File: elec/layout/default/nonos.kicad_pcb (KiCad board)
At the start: 2 copper layers, 4 parts, among them CN1 HRSHirose_DF40C_100DS_0_4V51, CN2 HRSHirose_DF40C_100DS_0_4V51, U1 _Texas_Instruments_SN74LVC1G0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

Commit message: refactor for core updates
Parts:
- added R1: , lcsc:R0402, F.Cu at (109.6, 28.8)
- added R2: 453Ω ±1% 62.5mW, lcsc:R0402, F.Cu at (104.4, 29.8)
- added RJ1: _HANRUNZhongshan_HanRun_Elec_HR911130A, lcsc:RJ45-TH_HR911130A, F.Cu at (168.2, 65.2)
- moved CN2 195.9 mm to (162.4, 104.6)
- moved CN1 145.0 mm to (125.6, 72.4)
- moved D1 112.4 mm to (103.8, 33.0)
- moved U1 34.0 mm to (138.4, 94.2)
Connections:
- net pins[23] renamed processor.hdi_b-pins[23]
- net pins[28] renamed processor.hdi_b-pins[28]
- net pins[33] renamed processor.hdi_b-pins[33]
- net pins[46] renamed processor-pins[46]
- net processor-signal-11 renamed pins[55]
- net processor.hdi_b-pins[38] renamed pins[38]
- net processor.hdi_b-pins[40] renamed pins[40]
- CN1 pad 12: processor-signal-3 -> processor-pins[23]
- CN1 pad 15: processor-signal-9 -> processor-signal-5
- CN1 pad 17: processor-signal-5 -> processor-pins[33]
- CN1 pad 22: processor-signal-1 -> pins[43]
- CN1 pad 23: processor-signal-10 -> processor-signal-8
- CN1 pad 24: pins[47] -> processor-signal-6
- CN1 pad 27: pins[53] -> processor-signal-3
- CN1 pad 29: processor-signal -> pins[57]
- CN1 pad 77: processor-signal-8 -> processor-pins[46]-1
- CN1 pad 78: processor-signal-6 -> processor-signal-2
- CN1 pad 80: processor-pins[40] -> processor-signal
- CN1 pad 81: processor-pins[38] -> processor-signal-9
- CN1 pad 82: processor-signal-12 -> processor-signal-7
- CN1 pad 85: processor-signal-7 -> processor-signal-4
- CN1 pad 86: processor-signal-4 -> processor-pins[28]
- CN1 pad 87: processor-signal-2 -> processor-signal-1
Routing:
- net (no net): track 5.67 -> 0.00 mm, vias 55 -> 0
- net GND: track 0.48 -> 0.00 mm, vias 35 -> 0

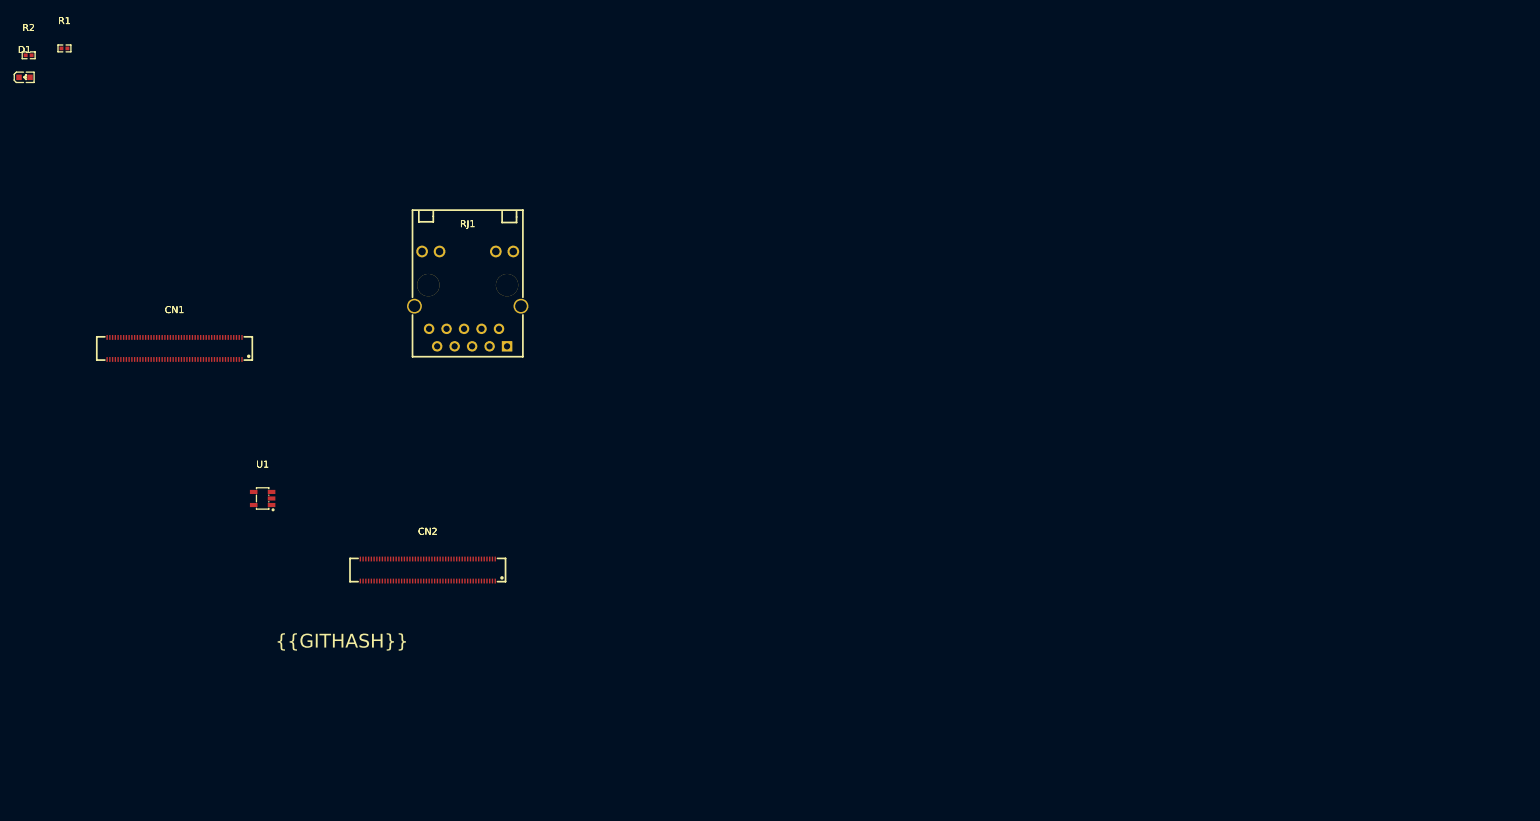
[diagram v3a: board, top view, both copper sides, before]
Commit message: rename pdcontroller folder
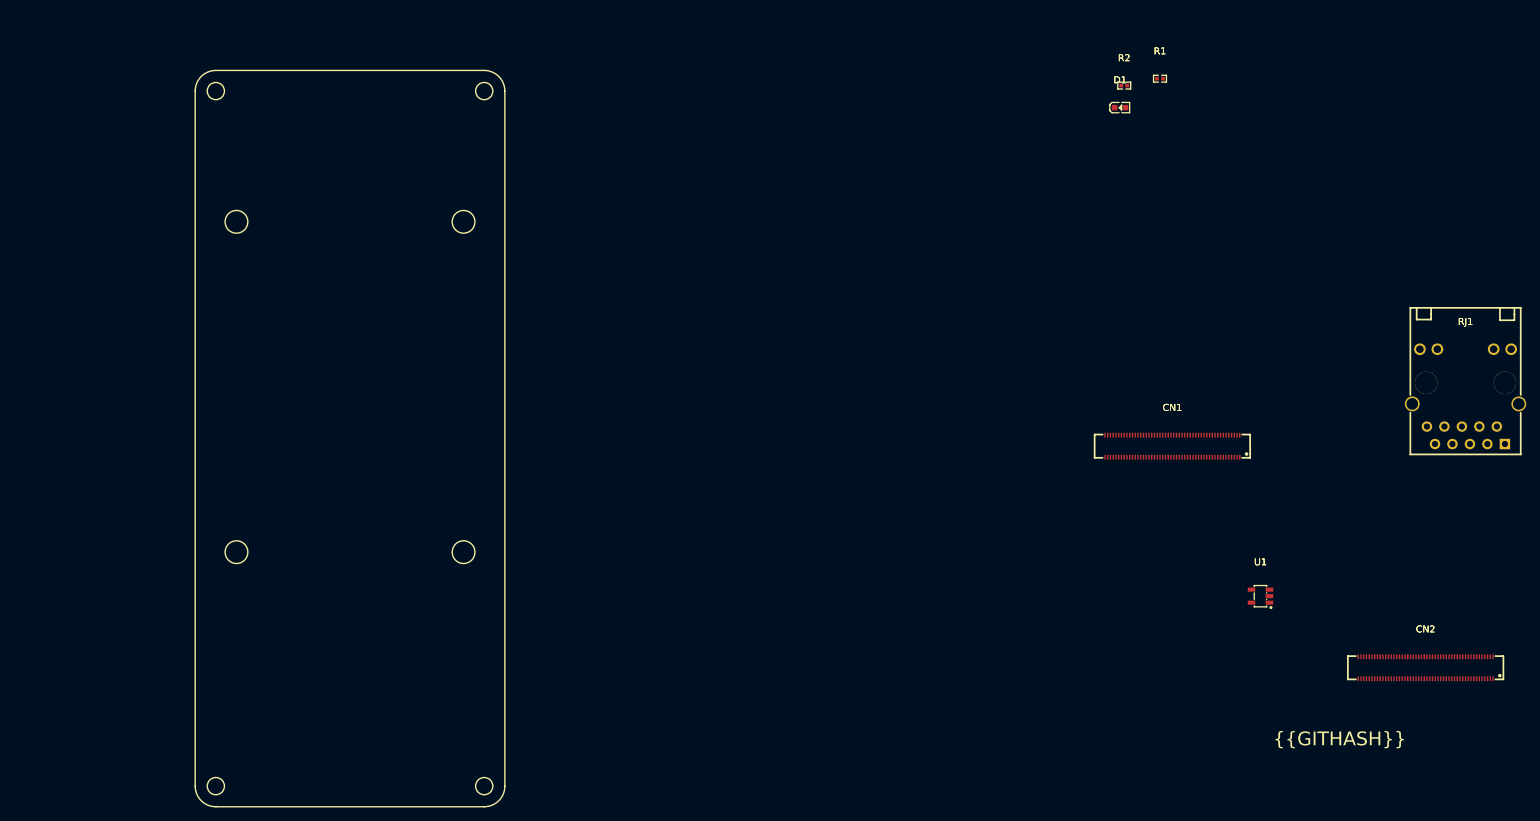
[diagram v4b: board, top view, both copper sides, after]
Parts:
- moved R1 159.3 mm to (268.8, 33.2)
- moved R2 159.3 mm to (263.6, 34.2)
- moved D1 159.3 mm to (263.0, 37.4)
- moved CN1 145.7 mm to (270.6, 86.6)
- moved RJ1 145.7 mm to (313.2, 79.4)
- moved CN2 145.7 mm to (307.4, 118.8)
- moved U1 145.7 mm to (283.4, 108.4)
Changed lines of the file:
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@@
 	(footprint "lcsc:CONN-SMD_DF40C-100DS-0.4V-51"
 		(layer "F.Cu")
-		(at 162.4 104.6)
+		(at 307.4 118.8)
 		(property "Reference" "CN2"
 			(at 0 -5.6 0)
@@
 	(footprint "lcsc:CONN-SMD_DF40C-100DS-0.4V-51"
 		(layer "F.Cu")
-		(at 125.6 72.4)
+		(at 270.6 86.6)
 		(property "Reference" "CN1"
 			(at 0 -5.6 0)
@@
 	(footprint "lcsc:LED0603-RD_WHITE"
 		(layer "F.Cu")
-		(at 103.8 33)
+		(at 263 37.4)
 		(property "Reference" "D1"
 			(at 0 -4 0)
@@
 	(footprint "lcsc:SOT-23-5_L3.0-W1.7-P0.95-LS2.8-BR"
 		(layer "F.Cu")
-		(at 138.4 94.2)
+		(at 283.4 108.4)
 		(property "Reference" "U1"
 			(at 0 -4.95 0)
@@
 	(footprint "lcsc:RJ45-TH_HR911130A"
 		(layer "F.Cu")
-		(at 168.2 65.2)
+		(at 313.2 79.4)
 		(property "Reference" "RJ1"
 			(at 0 -10.89 0)
@@
 	(footprint "lcsc:R0402"
 		(layer "F.Cu")
-		(at 109.6 28.8)
+		(at 268.8 33.2)
 		(property "Reference" "R1"
 			(at 0 -4 0)
@@
 	(footprint "lcsc:R0402"
 		(layer "F.Cu")
-		(at 104.4 29.8)
+		(at 263.6 34.2)
 		(property "Reference" "R2"
 			(at 0 -4 0)
@@
 		)
 	)
+	(gr_arc
+		(start 128.6 35)
+		(mid 129.47868 32.87868)
+		(end 131.6 32)
+		(stroke
+			(width 0.2)
+			(type default)
+		)
+		(layer "F.SilkS")
+	)
+	(gr_arc
+		(start 173.6 135.999999)
+		(mid 172.72132 138.12132)
+		(end 170.599999 139)
+		(stroke
+			(width 0.2)
+			(type default)
+		)
+		(layer "F.SilkS")
+	)
+	(gr_circle
+		(center 170.6 35)
+		(end 170.6 33.75)
+		(stroke
+			(width 0.2)
+			(type default)
+		)
+		(fill none)
+		(layer "F.SilkS")
+	)
+	(gr_line
+		(start 170.6 32)
+		(end 131.6 32)
+		(stroke
+			(width 0.2)
+			(type default)
+		)
+		(layer "F.SilkS")
+	)
+	(gr_circle
+		(center 134.599999 102)
+		(end 134.599999 100.35)
+		(stroke
+			(width 0.2)
+			(type default)
+		)
+		(fill none)
+		(layer "F.SilkS")
+	)
+	(gr_circle
+		(center 167.599999 102)
+		(end 167.599999 100.35)
+		(stroke
+			(width 0.2)
+			(type default)
+		)
+		(fill none)
+		(layer "F.SilkS")
+	)
+	(gr_arc
+		(start 170.6 32)
+		(mid 172.72132 32.87868)
+		(end 173.6 35)
+		(stroke
+			(width 0.2)
+			(type default)
+		)
+		(layer "F.SilkS")
+	)
+	(gr_line
+		(start 128.6 35)
+		(end 128.6 135.999999)
+		(stroke
+			(width 0.2)
+			(type default)
+		)
+		(layer "F.SilkS")
+	)
+	(gr_circle
+		(center 167.599999 54)
+		(end 167.599999 52.35)
+		(stroke
+			(width 0.2)
+			(type default)
+		)
+		(fill none)
+		(layer "F.SilkS")
+	)
+	(gr_circle
+		(center 131.6 35)
+		(end 131.6 33.75)
+		(stroke
+			(width 0.2)
+			(type default)
+		)
+		(fill none)
+		(layer "F.SilkS")
+	)
+	(gr_line
+		(start 131.600001 139)
+		(end 170.599999 139)
+		(stroke
+			(width 0.2)
+			(type default)
+		)
+		(layer "F.SilkS")
+	)
+	(gr_arc
+		(start 131.600001 139)
+		(mid 129.47868 138.12132)
+		(end 128.6 135.999999)
+		(stroke
+			(width 0.2)
+			(type default)
+		)
+		(layer "F.SilkS")
+	)
+	(gr_line
+		(start 173.6 135.999999)
+		(end 173.6 35)
+		(stroke
+			(width 0.2)
+			(type default)
+		)
+		(layer "F.SilkS")
+	)
+	(gr_circle
+		(center 134.5964 54)
+		(end 134.5964 52.35)
+		(stroke
+			(width 0.2)
+			(type default)
+		)
+		(fill none)
+		(layer "F.SilkS")
+	)
+	(gr_circle
+		(center 131.6 136)
+		(end 131.6 134.75)
+		(stroke
+			(width 0.2)
+			(type default)
+		)
+		(fill none)
+		(layer "F.SilkS")
+	)
+	(gr_circle
+		(center 170.6 136)
+		(end 170.6 134.75)
+		(stroke
+			(width 0.2)
+			(type default)
+		)
+		(fill none)
+		(layer "F.SilkS")
+	)
 	(gr_text "{{GITHASH}}"
-		(at 140.240427 116.111573 0)
+		(at 285.240427 130.311573 0)
 		(layer "F.SilkS")
 		(effects
@@
 		)
 	)
+	(group ""
+		(members "08449fd7-3562-4a6b-82dc-82238bd60984" "15c6fab9-3c42-4d6f-8911-c5026ce38e25"
+			"2d91a9ed-0909-4e89-95aa-87d2f383551e" "318d769f-56d3-42ae-8031-b2163136a6e9"
+			"31e3f335-7495-4d33-964e-ec2a7883306c" "3337c282-a3b1-45bf-8b25-ad2a3cf1ac43"
+			"35cb150f-111c-444d-86a2-8095a220c0b6" "3857a144-f54a-406b-b12f-fa8aea3b459e"
+			"5632c9c1-b1d7-4ee4-973f-3d0a5f52a530" "578e32bc-3a05-4bcf-90be-c9fa412d148c"
+			"747c8e98-96d1-407f-a33c-7eee050ed050" "8262d93c-2ac8-4ca9-bff9-39d09bf63ad6"
+			"87a79ec9-6d5f-4355-8631-b491081f022c" "97071fcc-94d5-4969-9521-23979f6ce8b0"
+			"cdf9749b-7d64-4d01-ad7c-d4c707002045" "e1a8b1c1-6317-4fb5-ab02-c4ae83287e97"
+		)
+	)

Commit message: layout sync working
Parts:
- added C1: 4.7µF ±10% 35V X5R, lcsc:C0603, F.Cu at (88.9, 131.4)
- added C2: 100nF ±10% 10V X5R, lcsc:C0201, F.Cu at (94.8, 122.0)
- added C3: 1µF ±20% 6.3V X5R, lcsc:C0201, F.Cu at (94.6, 124.7)
- added C4: , lcsc:C0201, F.Cu at (94.5, 125.7)
- added D2: , lcsc:DFN1610-2_L1.6-W1.0-P1.05-RD, F.Cu at (89.6, 128.6)
- added D3: , lcsc:DFN1610-2_L1.6-W1.0-P1.05-RD, F.Cu at (89.6, 125.6)
- added D4: 2.7V, lcsc:LED0603-RD_WHITE, F.Cu at (121.0, 105.5)
- added Q1: MOSFET, lcsc:SOT-23-3_L2.9-W1.3-P1.90-LS2.4-BR, F.Cu at (92.1, 127.7)
- added R3: , lcsc:R0201, F.Cu at (101.1, 126.1)
- added R4: 1kΩ ±1% 50mW, lcsc:R0201, F.Cu at (94.8, 123.2)
- added R5: 100kΩ ±1% 50mW, lcsc:R0201, F.Cu at (96.0, 121.3)
- added R6: 22.1kΩ ±1% 50mW, lcsc:R0201, F.Cu at (97.1, 122.0)
- added R7: 100Ω ±1% 50mW, lcsc:R0201, F.Cu at (96.0, 122.0)
- added R8: 453Ω ±1% 62.5mW, lcsc:R0402, F.Cu at (178.9, 131.1)
- added R9: , lcsc:R0402, F.Cu at (161.8, 135.9)
- added U2: _Texas_Instruments_SN74LVC1G07DBVR, lcsc:SOT-23-5_L3.0-W1.7-P0.95-LS2.8-BR, F.Cu at (121.2, 97.9)
- added USB1: TYPE_C_16PIN_2MD073, lcsc:USB-C-SMD_TYPE-C-6PIN-2MD-073, F.Cu at (94.7, 133.1)
- D1: value 2.7V -> ESDA25W; footprint lcsc:LED0603-RD_WHITE -> lcsc:SOT-323-3_L2.1-W1.3-P1.32-LS2.1-BR
- R1: footprint lcsc:R0402 -> lcsc:R0201
- R2: value 453Ω ±1% 62.5mW -> 4.64kΩ ±1% 50mW; footprint lcsc:R0402 -> lcsc:R0201
- U1: value _Texas_Instruments_SN74LVC1G07DBVR -> STUSB4500QTR; footprint lcsc:SOT-23-5_L3.0-W1.7-P0.95-LS2.8-BR -> lcsc:QFN-24_L4.0-W4.0-P0.50-BL-EP2.8
- moved R1 191.1 mm to (101.1, 124.9), turned to 180 degrees
- moved D1 191.0 mm to (95.0, 128.2), turned to -90 degrees
- moved R2 187.1 mm to (101.1, 127.0)
- moved U1 186.3 mm to (97.8, 125.1)
- moved RJ1 167.6 mm to (152.7, 127.8), turned to 180 degrees
- moved CN2 143.6 mm to (168.1, 84.0), turned to 90 degrees
- moved CN1 136.5 mm to (134.1, 84.0), turned to 90 degrees
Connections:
- net gnd renamed pd_controller.PD_CONTROLLER.footprint.pins[18].net-net
- net pins[26] renamed processor.hdi_b-pins[26]
- net pins[40] renamed processor.hdi_b-pins[40]
- net pins[54] renamed processor-signal-11
- net processor-pins[27] renamed processor-signal-12
- net processor.hdi_b-pins[27] renamed pins[27]
- net processor.hdi_b-pins[28] renamed pins[28]
- net processor.hdi_b-pins[33] renamed pins[33]
- net processor.hdi_b-pins[49] renamed pins[49]
- CN1 pad 15: processor-signal-5 -> processor-signal-10
- CN1 pad 17: processor-pins[33] -> processor-signal-7
- CN1 pad 19: pins[37] -> processor-signal-2
- CN1 pad 23: processor-signal-8 -> processor-signal-9
- CN1 pad 24: processor-signal-6 -> pins[47]
- CN1 pad 25: processor-pins[49] -> processor-signal-6
- CN1 pad 29: pins[57] -> processor-signal-1
- CN1 pad 75: pins[50] -> processor-signal-8
- CN1 pad 77: processor-pins[46]-1 -> processor-pins[46]
- CN1 pad 78: processor-signal-2 -> processor-signal-4
- CN1 pad 80: processor-signal -> processor-pins[40]
- CN1 pad 81: processor-signal-9 -> processor-signal-5
- CN1 pad 82: processor-signal-7 -> pins[36]
- CN1 pad 85: processor-signal-4 -> pins[30]
- CN1 pad 86: processor-pins[28] -> processor-signal
- CN1 pad 87: processor-signal-1 -> processor-pins[26]
- CN2 pad 77: processor-pins[46] -> processor-pins[46]-1
- D1 pad 1: net -> CC1
- D1 pad 2: VCC_3V3 -> CC2
- R1 pad 1: VCC_3V3 -> VBUS
- R1 pad 2: rj45-net-1 -> pd_controller-net-4
- R2 pad 1: VCC_3V3 -> I2C_SCL
- R2 pad 2: rj45-net -> hv
- U1 pad 1: n_c_ -> CC1
- U1 pad 2: PWR_LED -> CC1
- U1 pad 4: net -> CC2
- U1 pad 5: VCC_3V3 -> CC2
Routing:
- net VBUS: track 0.00 -> 24.6 mm, vias 0 -> 11
- net I2C_SCL: track 0.00 -> 15.2 mm, vias 0 -> 2
- net pd_controller-lv: track 0.00 -> 12.7 mm, vias 0 -> 30
- net pd_controller-net: track 0.00 -> 12.1 mm, vias 0 -> 2
- net I2C_SDA: track 0.00 -> 11.6 mm, vias 0 -> 2
- net hv: track 0.00 -> 10.1 mm
- net CC2: track 0.00 -> 5.99 mm
- net CC1: track 0.00 -> 5.72 mm
- net VSINK_VCC: track 0.00 -> 4.79 mm
- net pd_controller.USB_CONNECTOR-net: track 0.00 -> 2.72 mm
- net pd_controller.USB_CONNECTOR-net-1: track 0.00 -> 2.72 mm
- net pd_controller-net-2: track 0.00 -> 1.52 mm
- net pd_controller-net-4: track 0.00 -> 1.26 mm
- net pd_controller-net-3: track 0.00 -> 1.22 mm
- net VREG_1V2: track 0.00 -> 1.04 mm
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- added copper zone on B.Cu, net VBUS
- added copper zone on F.Cu, net VBUS
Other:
- board text added: "USBPD DEV BOARD"
